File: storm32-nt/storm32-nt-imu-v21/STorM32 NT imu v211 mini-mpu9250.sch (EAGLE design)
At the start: 13 parts, among them IC1 STM32F10XTXU6, Q1 RESONATORSMD

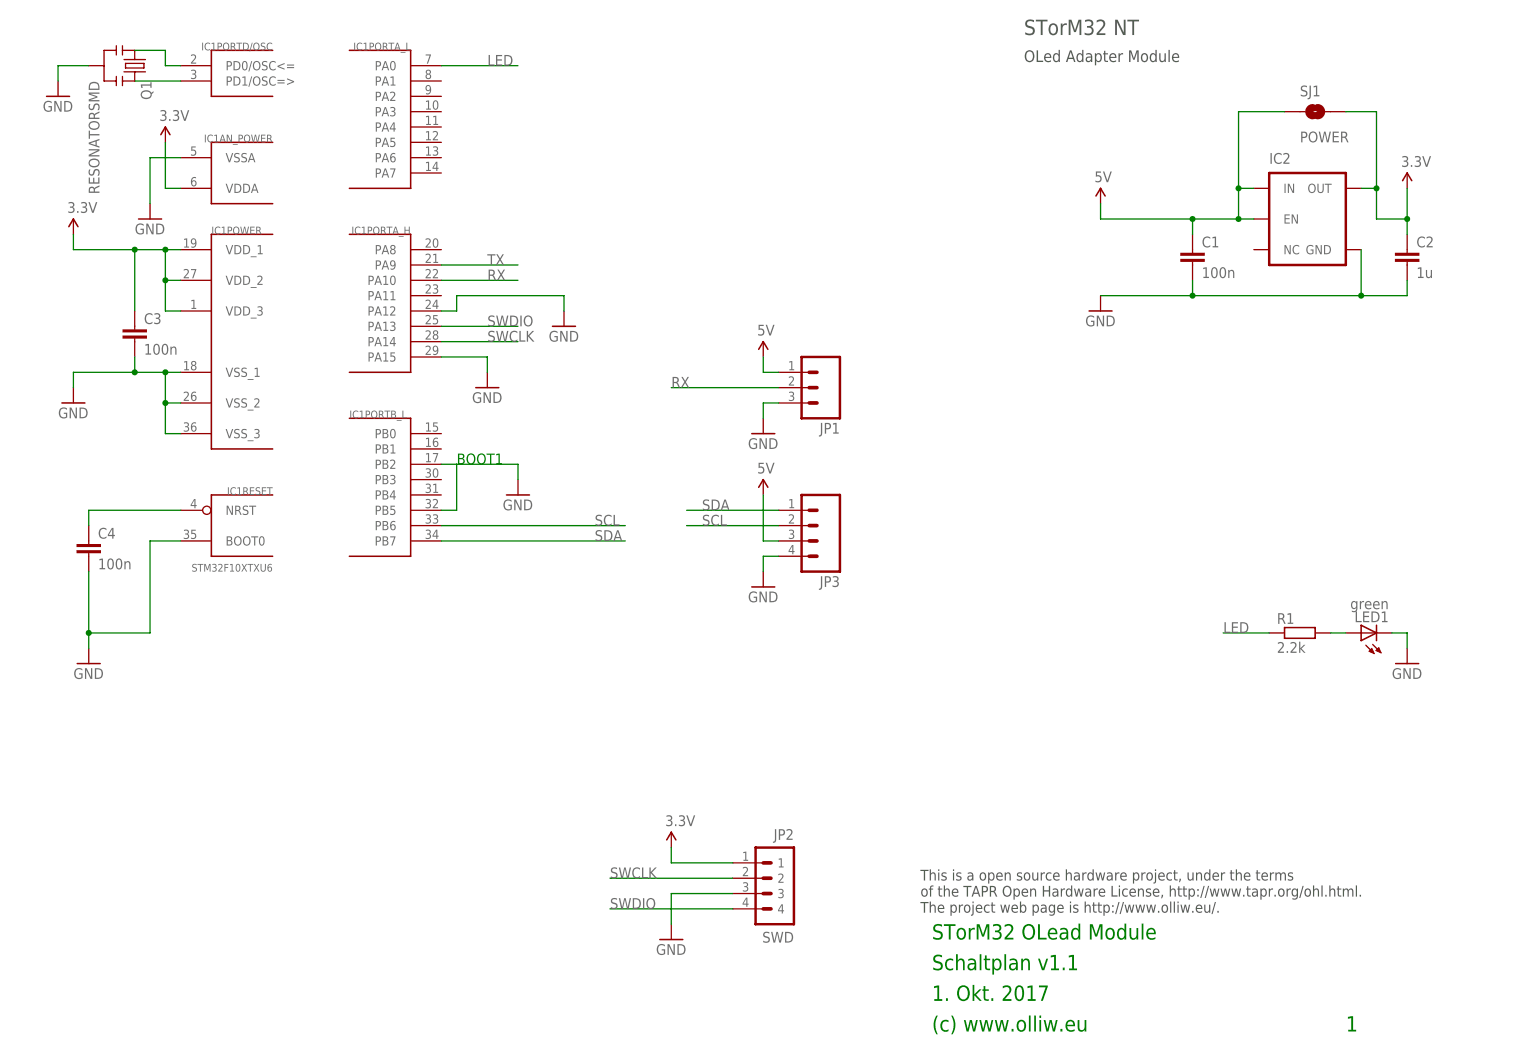
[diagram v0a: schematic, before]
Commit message: release NT imu v2.11, NT encoder motor v2.51E, display v1.3
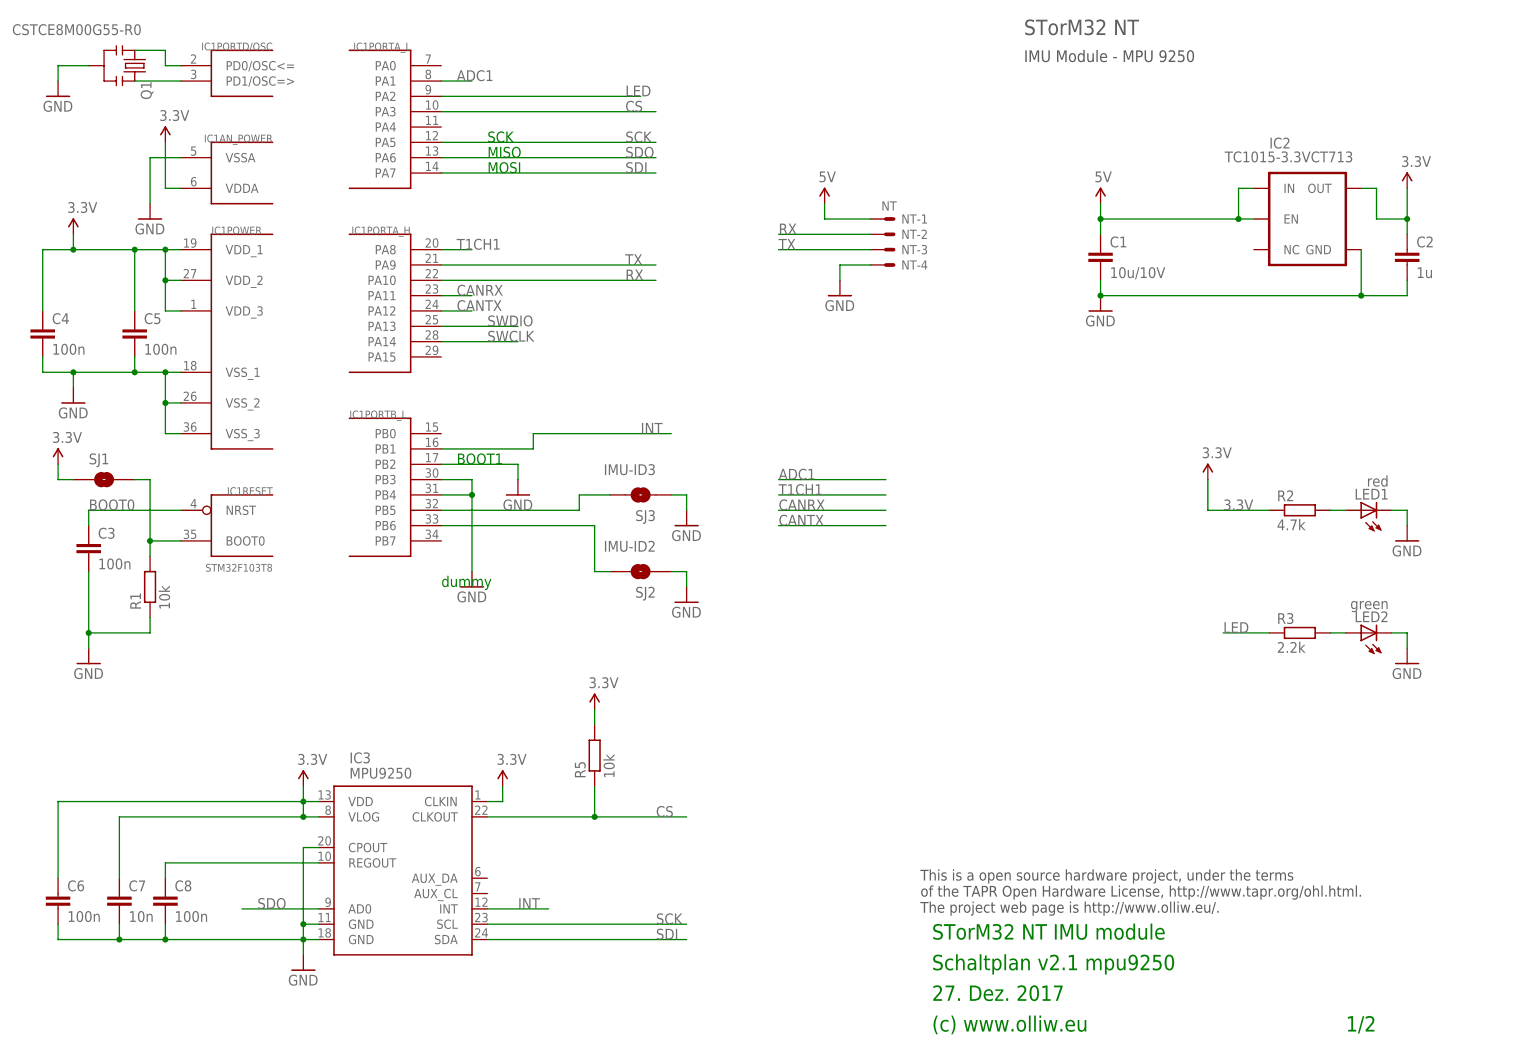
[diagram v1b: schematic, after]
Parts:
- removed JP1: (no value), # SparkFun2:M03PTH
- removed JP2: SWD, # stdlib:P4X1_1P27-OCT_BILEX
- removed JP3: (no value), # SparkFun2:M04PTH
- added C5, C6, C8: 100n, rcl:C-EUC0402
- added C7: 10n, rcl:C-EUC0402
- added IC3: MPU9250, # SparkFun2:IMU3000QFN-24-0.4MIL
- added LED2: green, led:LEDCHIPLED_0603
- added NT: NT, con-jst2:SM04B-SRSS-TB
- added R2: 4.7k, rcl:R-EU_R0402
- added R3: 2.2k, rcl:R-EU_R0402
- added R5: 10k, rcl:R-EU_R0402
- added SJ2: IMU-ID2, # SparkFun2:SOLDERJUMPERNO
- added SJ3: IMU-ID3, # SparkFun2:SOLDERJUMPERNO
- C1: value 100n -> 10u/10V; device rcl:C-EUC0603 -> rcl:C-EUC0805
- C3, C4: device rcl:C-EUC0603 -> rcl:C-EUC0402
- IC1: value STM32F10XTXU6 -> STM32F103T8
- IC2: value (none) -> TC1015-3.3VCT713
- LED1: value green -> red
- Q1: value RESONATORSMD -> CSTCE8M00G55-R0
- R1: value 2.2k -> 10k; device rcl:R-EU_R0603 -> rcl:R-EU_R0402
- SJ1: value POWER -> BOOT0
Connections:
- removed net SCL: IC1PORTB_L.PB6, JP3.2
- removed net SDA: IC1PORTB_L.PB7, JP3.1
- new net ADC1: IC1PORTA_L.PA1
- new net CANRX: IC1PORTA_H.PA11
- new net CANTX: IC1PORTA_H.PA12
- new net CS: IC1PORTA_L.PA3, IC3.CLKOUT, R5.1
- new net INT: IC1PORTB_L.PB1, IC3.INT
- new net N$20: C8.1, IC3.REGOUT
- new net N$3: IC1RESET.BOOT0, R1.2, SJ1.2
- new net N$4: IC1PORTB_L.PB5, SJ3.2
- new net N$7: IC1PORTB_L.PB6, SJ2.2
- new net N$9: LED1.A, R2.2
- new net SCK: IC1PORTA_L.PA5, IC3.SCL
- new net SDI: IC1PORTA_L.PA7, IC3.SDA
- new net SDO: IC1PORTA_L.PA6, IC3.AD0
- new net T1CH1: IC1PORTA_H.PA8
- net 3.3V: now also C4.1, C5.1, C6.1, C7.1, IC3.CLKIN, IC3.VDD, IC3.VLOG, R2.1, R5.2, SJ1.1; no longer C3.1, JP2.1, SJ1.2
- net 5V: now also NT-1.S; no longer JP1.1, JP3.3, SJ1.1
- net GND: now also C5.2, C6.2, C7.2, C8.2, IC1PORTB_L.PB3, IC1PORTB_L.PB4, IC3.CPOUT, IC3.GND@11, IC3.GND@18, LED2.C, NT-4.S, R1.1, SJ2.1, SJ3.1; no longer IC1PORTA_H.PA12, IC1PORTA_H.PA15, IC1PORTB_L.PB5, IC1RESET.BOOT0, JP1.3, JP2.3, JP3.4
- net LED: now also IC1PORTA_L.PA2, R3.1; no longer IC1PORTA_L.PA0, R1.1
- net N$1: now also C3.1; no longer C4.1
- net N$2: now also LED2.A, R3.2; no longer LED1.A, R1.2
- net RX: now also NT-2.S; no longer JP1.2
- net SWCLK: no longer JP2.2
- net SWDIO: no longer JP2.4
- net TX: now also NT-3.S
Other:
- note added: "1/2"
- note added: "27. Dez. 2017"
- note added: "IMU Module - MPU 9250"
- note added: "MISO"
- note added: "MOSI"
- note added: "SCK"
- note added: "STorM32 NT IMU module"
- note added: "Schaltplan v2.1 mpu9250"
- note added: "dummy"
- note removed: "1"
- note removed: "1. Okt. 2017"
- note removed: "OLed Adapter Module"
- note removed: "STorM32 OLead Module"
- note removed: "Schaltplan v1.1"
- moved on the sheet: C1, C3, C4, LED1, R1, SJ1
